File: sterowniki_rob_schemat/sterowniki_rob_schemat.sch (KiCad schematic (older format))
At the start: 10 parts, among them Q1 Q_NPN_BCE, U1 STM32L476VGTx, U2 LSM303D

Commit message: schemat v0.2
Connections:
- net +3V3 is gone; now on net 3V3: U2.1 (VDDIO)
- net +5V: no longer 100n.1, S1.1 (V++), S2.1 (V++), S3.1 (V++), S4.1 (V++)
- net 0: now also U1.99 (VSS)
- net at S1.2 (Trig): now also U1.37 (PB2); no longer U1.47 (PB10)
- net at S1.3 (Echo): now also U1.36 (PB1); no longer U1.23 (PA0)
- net at U1.86 (PD5): no longer U2.4 (SCL/SPC)
- net at U1.15 (PC0): now also S4.3 (Echo)
- net at U1.16 (PC1): now also S4.2 (Trig)
- net at U1.18 (PC3): now also S2.2 (Trig)
- net 3V3: now reaches U1.22 (VDDA)
- net at U1.24 (PA1): no longer S2.3 (Echo)
- net at U1.25 (PA2): no longer S3.3 (Echo)
- net acc: now reaches U1.31 (PA6)
- net acc: now also U2.4 (SCL/SPC); no longer S4.3 (Echo)
- net at U1.32 (PA7): now also S3.3 (Echo)
- net at U1.33 (PC4): now also S3.2 (Trig)
- net at U1.34 (PC5): now also S2.3 (Echo)
- net at U1.48 (PB11): no longer S2.2 (Trig)
- net at U1.5 (PE6): no longer Q1.1 (B)
- net at U1.52 (PB13): no longer S3.2 (Trig)
- net at U1.53 (PB14): no longer S4.2 (Trig)
- net 5V: now reaches U1.75 (VDD)
- net 5V: now also 100n.1, S1.1 (V++), S2.1 (V++), S3.1 (V++), S4.1 (V++)
- net buzzer: now reaches U1.93 (PB7)
- net buzzer: now also Q1.1 (B)
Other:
- moved on the sheet: 100n, BZ1, Q1, R?, S1, S2, S3, S4, U1, U2

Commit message: schemat polaczen etap II
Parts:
- removed S2, S3, S4: HC-SR04, symbol bib:HC-SR04
- removed U2: LSM303D, Package_LGA:LGA-16_3x3mm_P0.5mm, symbol Sensor_Motion:LSM303D
- gave numbers to parts that had none: 1
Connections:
- net +5V is gone; now on net 5V: R1.2
- net at S1.2 (Trig): now also U1.25 (PA2); no longer U1.37 (PB2)
- net at S1.3 (Echo): now also U1.23 (PA0); no longer U1.36 (PB1)
- net at U1.81 (PD0): now also Q1.1 (B)
- net acc: no longer names the net of U1.31 (PA6)
- net buzzer: no longer names the net of U1.93 (PB7)
- net buzzer: no longer Q1.1 (B)
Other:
- moved on the sheet: BZ1, Q1, R1

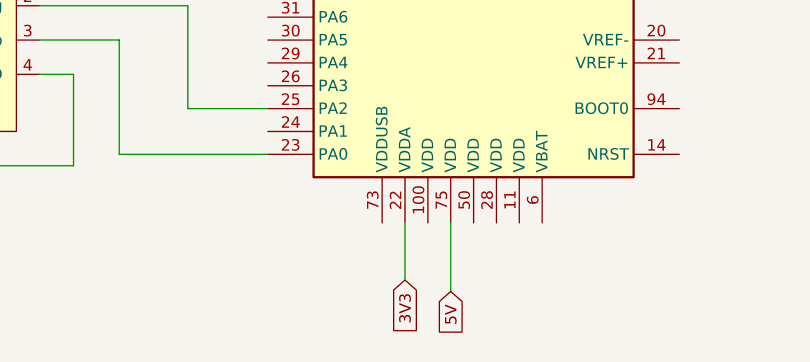
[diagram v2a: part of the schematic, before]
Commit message: schemat etap II popr
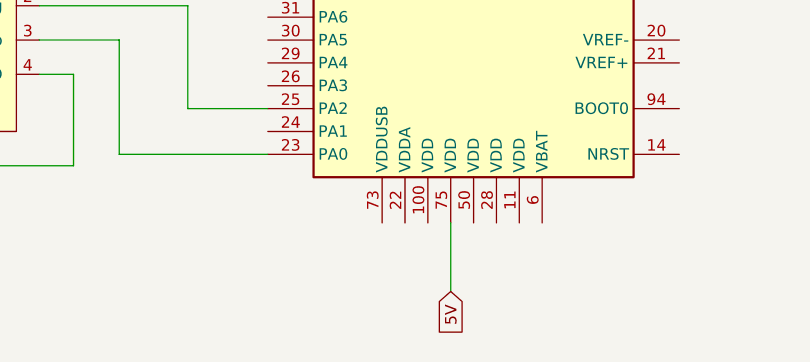
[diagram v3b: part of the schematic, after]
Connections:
- net 3V3: no longer names the net of U1.22 (VDDA)
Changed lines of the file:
@@
 Wire Wire Line
 	2850 6300 3200 6300
-Text GLabel 4450 7350 3    50   Input ~ 0
-3V3
 Text GLabel 4650 7400 3    50   Input ~ 0
 5V
@@
 Wire Wire Line
 	4650 7100 4650 7400
-Wire Wire Line
-	4450 7100 4450 7350
 $Comp
 L pspice:0 #GND?

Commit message: końcowy schemat układu
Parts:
- added S2, S3, S4: HC-SR04, symbol bib:HC-SR04
- added U? (x2): 74HC4051, symbol 74xx:74HC4051
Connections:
- net 0: now also S2.4 (GND), S3.4 (GND), S4.4 (GND)
- net 5V: now also S2.1 (V++), S3.1 (V++), S4.1 (V++), U?.16 (VCC), U?.16 (VCC)
- net at S1.2 (Trig): now also U?.13 (A0); no longer U1.25 (PA2)
- net at S1.3 (Echo): now also U?.13 (A0); no longer U1.23 (PA0)
- net PH0: now reaches U1.12 (PH0)
- net PH0: now also U1.13 (PH1), U?.11 (S0), U?.11 (S0)
- new net: U1.23 (PA0), U?.3 (A)
- new net: U1.25 (PA2), U?.3 (A)
- new net: S2.2 (Trig), U?.14 (A1)
- new net: S2.3 (Echo), U?.14 (A1)
- new net: S3.2 (Trig), U?.15 (A2)
- new net: S3.3 (Echo), U?.15 (A2)
- new net: S4.2 (Trig), U?.12 (A3)
- new net: S4.3 (Echo), U?.12 (A3)
- new net: U?.10 (S1), U?.10 (S1)
- new net GND: U?.8 (GND), U?.8 (GND)
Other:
- moved on the sheet: BZ1, Q1, R1, S1, U1

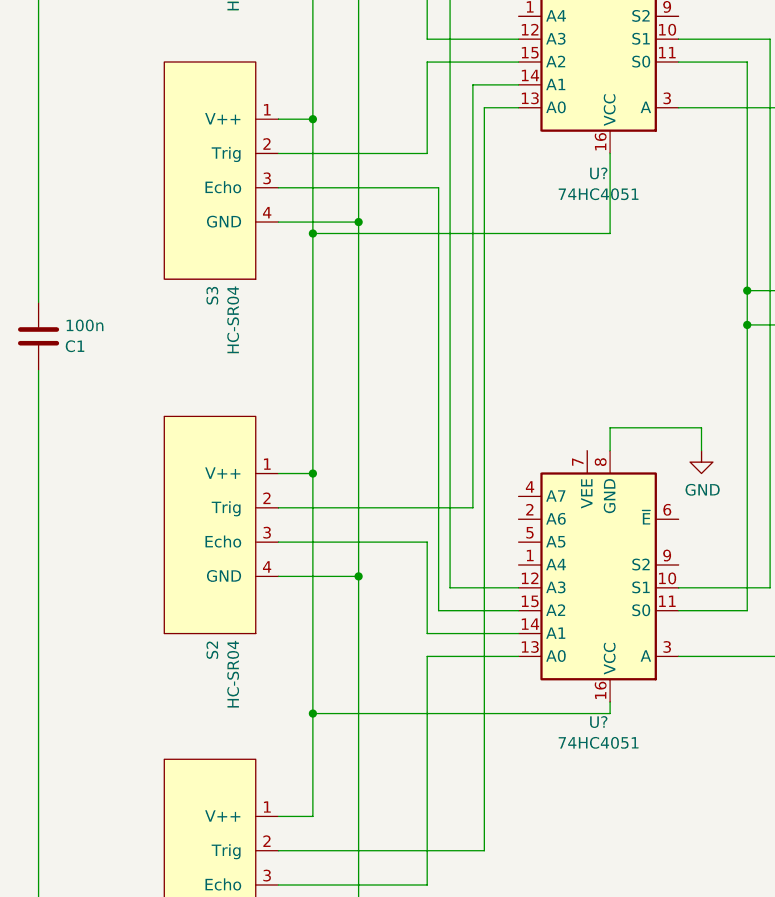
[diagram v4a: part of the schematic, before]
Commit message: schemat końcowy
poprawiono numerację na schemacie
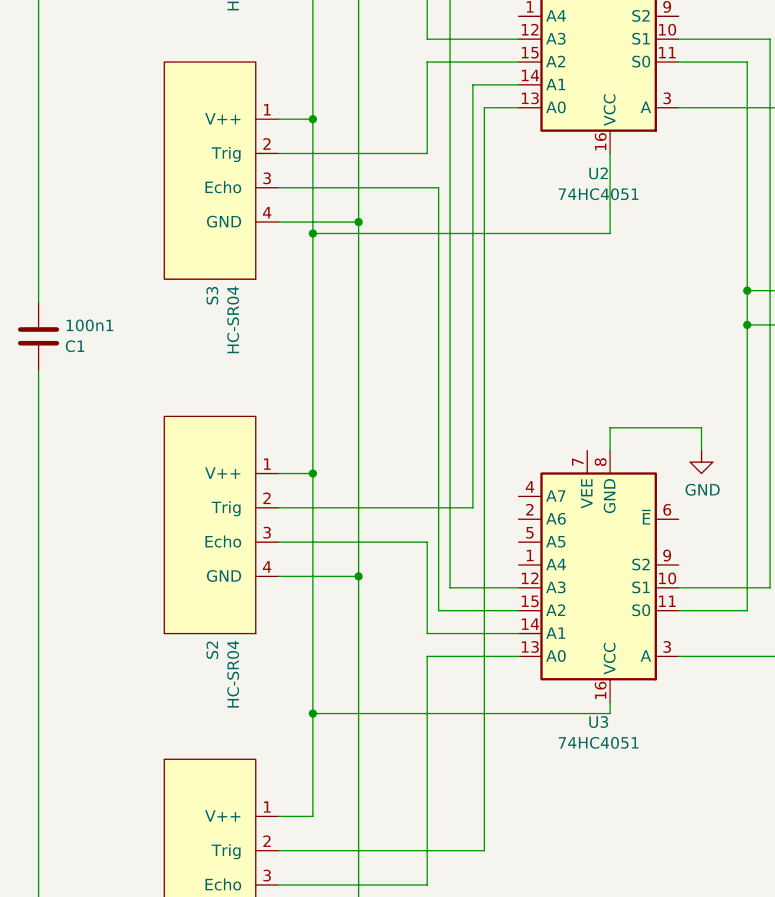
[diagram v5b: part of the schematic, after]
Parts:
- gave numbers to parts that had none: 2
- renumbered 100n to 100n1
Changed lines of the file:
@@
 	2500 6000 2350 6000
 $Comp
-L pspice:0 #GND?
+L pspice:0 #GND02
 U 1 1 624B547D
 P 2700 7050
-F 0 "#GND?" H 2700 6950 50  0001 C CNN
+F 0 "#GND02" H 2700 6950 50  0001 C CNN
 F 1 "0" H 2700 7139 50  0000 C CNN
 F 2 "" H 2700 7050 50  0001 C CNN
@@
 	8100 3100 8100 3250
 $Comp
-L pspice:0 #GND?
+L pspice:0 #GND04
 U 1 1 6248567F
 P 8100 3250
-F 0 "#GND?" H 8100 3150 50  0001 C CNN
+F 0 "#GND04" H 8100 3150 50  0001 C CNN
 F 1 "0" H 8150 3300 50  0000 C CNN
 F 2 "" H 8100 3250 50  0001 C CNN
@@
 	8100 2000 8100 1800
 $Comp
-L Device:C 100n
+L Device:C 100n1
 U 1 1 6249EA67
 P 1300 3900
-F 0 "100n" H 1415 3946 50  0000 L CNN
+F 0 "100n1" H 1415 3946 50  0000 L CNN
 F 1 "C1" H 1415 3855 50  0000 L CNN
 F 2 "" H 1338 3750 50  0001 C CNN
@@
 	1300 800  1300 3750
 $Comp
-L pspice:0 #GND?
+L pspice:0 #GND01
 U 1 1 624A30F7
 P 1300 7050
-F 0 "#GND?" H 1300 6950 50  0001 C CNN
+F 0 "#GND01" H 1300 6950 50  0001 C CNN
 F 1 "0" H 1300 7139 50  0000 C CNN
 F 2 "" H 1300 7050 50  0001 C CNN
@@
 	6350 6600 6350 6900
 $Comp
-L pspice:0 #GND?
+L pspice:0 #GND03
 U 1 1 625A9E28
 P 5850 1100
-F 0 "#GND?" H 5850 1000 50  0001 C CNN
+F 0 "#GND03" H 5850 1000 50  0001 C CNN
 F 1 "0" H 5850 1189 50  0000 C CNN
 F 2 "" H 5850 1100 50  0001 C CNN
@@
 	3000 1600 2350 1600
 $Comp
-L 74xx:74HC4051 U?
+L 74xx:74HC4051 U2
 U 1 1 628A8AFC
 P 3800 2600
-F 0 "U?" H 3850 3189 50  0000 C CNN
+F 0 "U2" H 3850 3189 50  0000 C CNN
 F 1 "74HC4051" H 3850 3280 50  0000 C CNN
 F 2 "" H 3800 2200 50  0001 C CNN
@@
 $EndComp
 $Comp
-L 74xx:74HC4051 U?
+L 74xx:74HC4051 U3
 U 1 1 628A57BB
 P 3800 5000
-F 0 "U?" H 3850 5589 50  0000 C CNN
+F 0 "U3" H 3850 5589 50  0000 C CNN
 F 1 "74HC4051" H 3850 5680 50  0000 C CNN
 F 2 "" H 3800 4600 50  0001 C CNN
@@
 PH1
 $Comp
-L power:GND #PWR?
+L power:GND #PWR01
 U 1 1 628E4B62
 P 4200 4400
-F 0 "#PWR?" H 4200 4150 50  0001 C CNN
+F 0 "#PWR01" H 4200 4150 50  0001 C CNN
 F 1 "GND" H 4205 4227 50  0000 C CNN
 F 2 "" H 4200 4400 50  0001 C CNN
@@
 $EndComp
 $Comp
-L power:GND #PWR?
+L power:GND #PWR02
 U 1 1 628E6171
 P 4250 2050
-F 0 "#PWR?" H 4250 1800 50  0001 C CNN
+F 0 "#PWR02" H 4250 1800 50  0001 C CNN
 F 1 "GND" H 4255 1877 50  0000 C CNN
 F 2 "" H 4250 2050 50  0001 C CNN

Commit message: schemat końcowy
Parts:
- removed S4: HC-SR04, symbol bib:HC-SR04
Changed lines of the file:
@@
-	0    -1   1    0
-$EndComp
-$Comp
-L bib:HC-SR04 S4
-U 1 1 6285209D
-P 2100 1550
-F 0 "S4" H 2728 1588 50  0000 L CNN
-F 1 "HC-SR04" H 2728 1497 50  0000 L CNN
-F 2 "" H 1800 1650 50  0001 C CNN
-F 3 "" H 1800 1650 50  0001 C CNN
-	1    2100 1550
 	0    -1   1    0
 $EndComp
@@
 Wire Wire Line
 	2350 6450 2700 6450
-Wire Wire Line
-	2350 1900 2700 1900
-Wire Wire Line
-	2700 1900 2700 3400
 Connection ~ 2700 6450
 Wire Wire Line
@@
 Wire Wire Line
 	2350 3400 2700 3400
-Connection ~ 2700 3400
 Wire Wire Line
 	2700 3400 2700 4950
-Wire Wire Line
-	2500 800  2500 1450
 Wire Wire Line
 	2500 4500 2350 4500
@@
 	2500 2950 2500 3450
 Wire Wire Line
-	2500 1450 2350 1450
-Connection ~ 2500 1450
-Wire Wire Line
-	2500 1450 2500 2950
-Wire Wire Line
 	2350 4800 3000 4800
 Wire Wire Line
 	3000 3100 2350 3100
-Wire Wire Line
-	3000 1600 2350 1600
 $Comp
 L 74xx:74HC4051 U2
@@
 	2350 3250 3050 3250
 Wire Wire Line
-	3400 5000 3100 5000
-Wire Wire Line
-	3100 5000 3100 1750
-Wire Wire Line
-	2350 1750 3100 1750
-Wire Wire Line
-	3000 1600 3000 2600
-Wire Wire Line
-	3000 2600 3400 2600
-Wire Wire Line
 	3000 3100 3000 2700
 Wire Wire Line
@@
 Wire Wire Line
 	2350 6150 3250 6150
+Wire Wire Line
+	2500 800  2500 2950
 $EndSCHEMATC
